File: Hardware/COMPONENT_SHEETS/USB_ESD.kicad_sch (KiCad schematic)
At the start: 9 parts, among them J4 10118192-0001LF, U4 LP38692MPX-ADJ, U5 USBLC6-2SC6

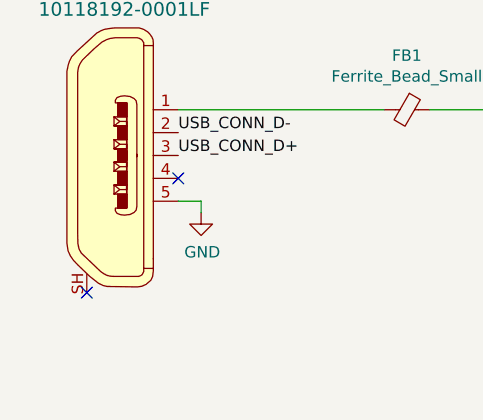
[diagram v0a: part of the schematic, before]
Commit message: fixed board update issue by renaming usb pin 0 and DSUB pin 0
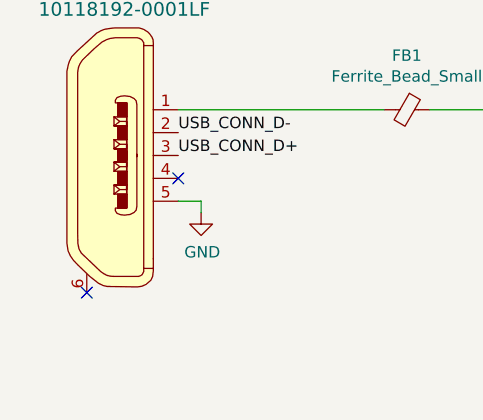
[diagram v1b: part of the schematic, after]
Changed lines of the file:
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@@
     (pin "4")
     (pin "5")
-    (pin "SH")
+    (pin "6")
   )
   (symbol (lib_id "Device:R_Small") (at 160.02 90.17 0) (unit 1)

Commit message: Updated USB connector part number based on manufacturer feedback
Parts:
- J4: LCSC C132564 -> C132560
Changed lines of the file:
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@@
       (effects (font (size 1.524 1.524)) (justify left) hide)
     )
-    (property "Datasheet" "http://www.amphenol-icc.com/media/wysiwyg/files/drawing/10118192.pdf" (id 3) (at 68.58 80.01 0)
+    (property "Datasheet" "https://www.molex.com/pdm_docs/sd/473460001_sd.pdf" (id 3) (at 68.58 80.01 0)
       (effects (font (size 1.524 1.524)) (justify left) hide)
     )
@@
       (effects (font (size 1.524 1.524)) (justify left) hide)
     )
-    (property "LCSC" "C132564" (id 13) (at 63.5 87.63 0)
+    (property "LCSC" "C132560" (id 13) (at 63.5 87.63 0)
       (effects (font (size 1.27 1.27)) hide)
     )

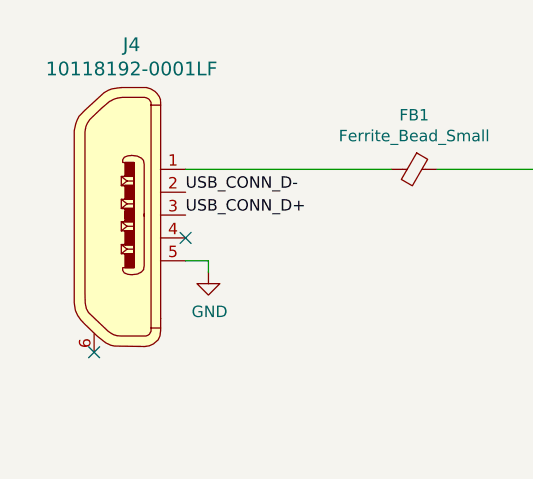
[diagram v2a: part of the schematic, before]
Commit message: Corrected USB footprint and moved USB edge cut
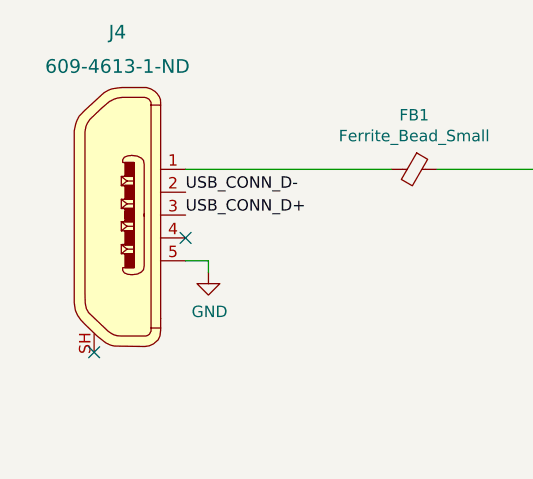
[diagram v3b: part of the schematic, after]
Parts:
- removed J4: 10118192-0001LF, Connector_USB:USB_Micro-B_Molex-105017-0001, symbol dk_USB-DVI-HDMI-Connectors:10118192-0001LF
- added J4: 609-4613-1-ND, digikeyUSBConnector:USB_Micro_B_Female_10118192, symbol USB:609-4613-1-ND
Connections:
- net GND: now also J4.5
- net USB_CONN_D+: now also J4.3
- net USB_CONN_D-: now also J4.2
- net at FB1.2: now also J4.1

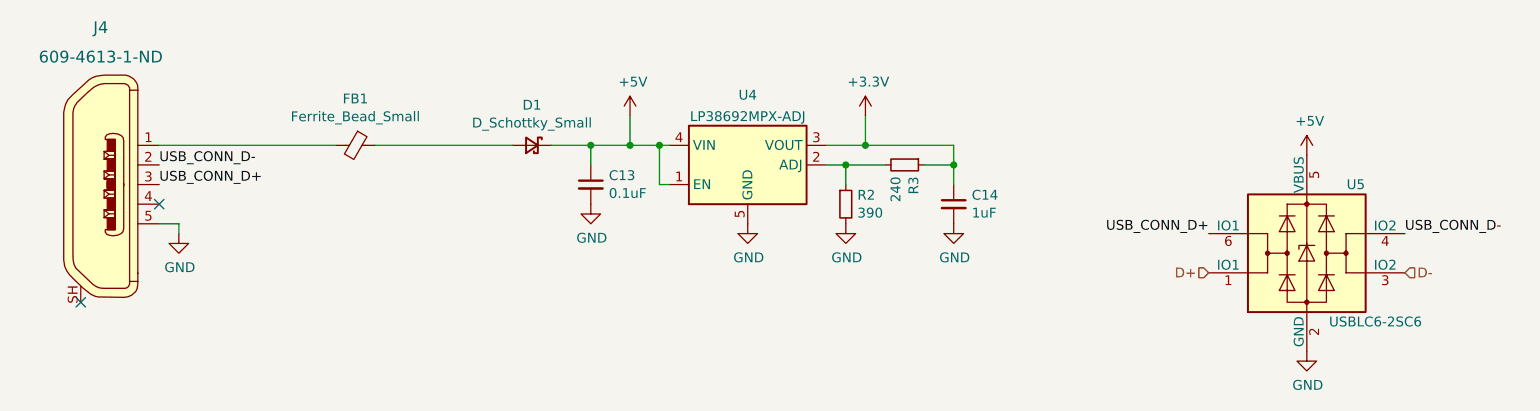
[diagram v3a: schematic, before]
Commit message: switched voltage regulator resistors
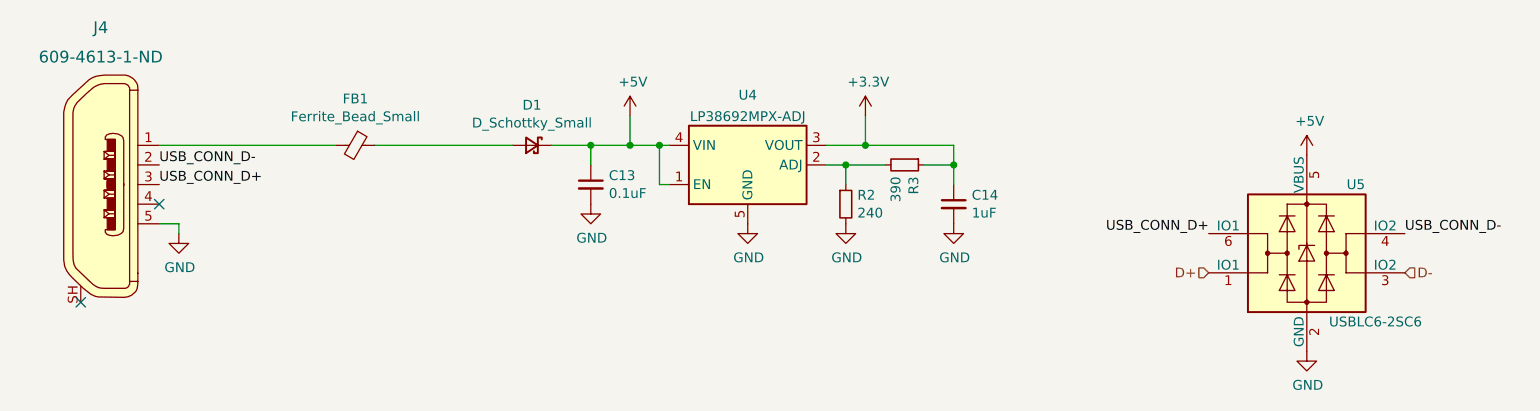
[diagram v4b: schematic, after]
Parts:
- R2: value 390 -> 240; LCSC C23151 -> C23350
- R3: value 240 -> 390; LCSC C23350 -> C23151
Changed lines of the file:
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@@
       (effects (font (size 1.27 1.27)) (justify left))
     )
-    (property "Value" "390" (id 1) (at 161.5186 91.313 0)
+    (property "Value" "240" (id 1) (at 161.5186 91.313 0)
       (effects (font (size 1.27 1.27)) (justify left))
     )
@@
       (effects (font (size 1.27 1.27)) hide)
     )
-    (property "LCSC" " C23151" (id 4) (at 160.02 90.17 0)
+    (property "LCSC" "C23350" (id 4) (at 160.02 90.17 0)
       (effects (font (size 1.27 1.27)) hide)
     )
@@
       (effects (font (size 1.27 1.27)) (justify left))
     )
-    (property "Value" "240" (id 1) (at 166.497 86.5886 0)
+    (property "Value" "390" (id 1) (at 166.497 86.5886 0)
       (effects (font (size 1.27 1.27)) (justify left))
     )
@@
       (effects (font (size 1.27 1.27)) hide)
     )
-    (property "LCSC" " C23350" (id 4) (at 167.64 85.09 0)
+    (property "LCSC" "C23151" (id 4) (at 167.64 85.09 0)
       (effects (font (size 1.27 1.27)) hide)
     )
